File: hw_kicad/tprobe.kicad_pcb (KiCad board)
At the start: 2 copper layers, 15.2 x 44.5 mm, 28 parts, among them IC1 ATTINY85-P, P1 INPUT, P2 PRB_GND, P3 PRB_VCC, P4 AVR_ISP, P5 FTDI_CN, P6 MLIPO, SW1 SW_PUSH_SMALL_H

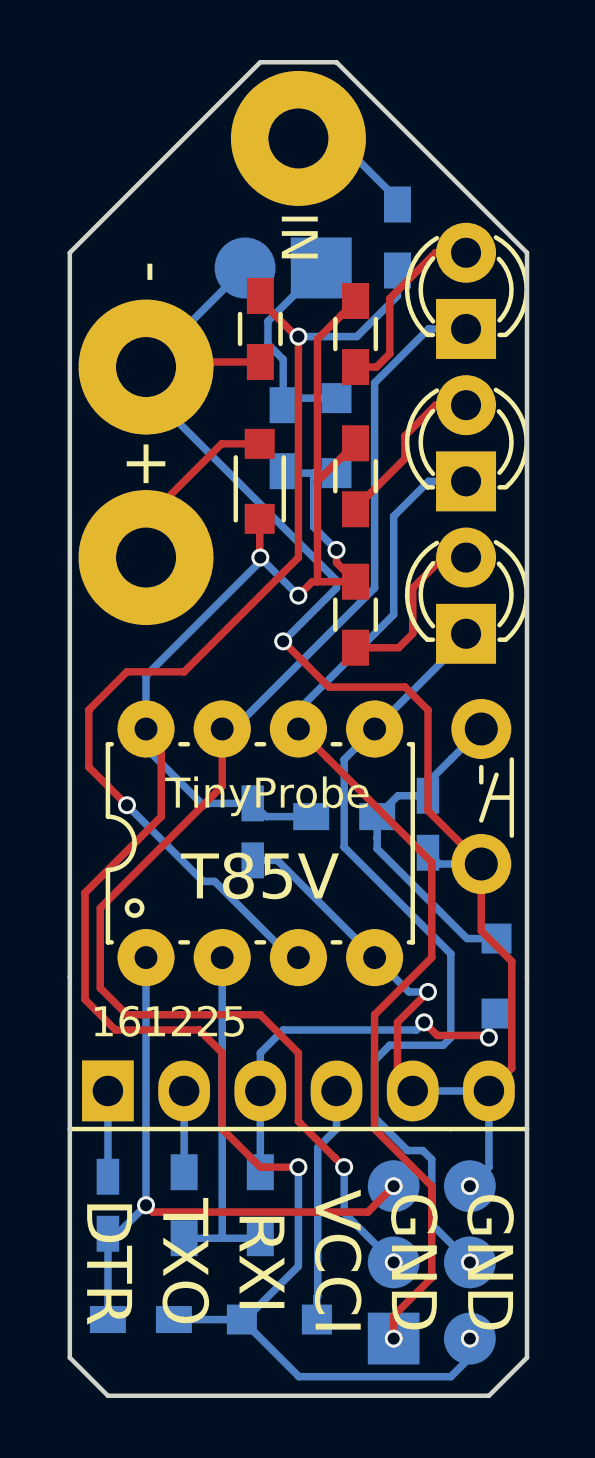
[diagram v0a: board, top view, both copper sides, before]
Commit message: It deserves a real li-ion charger :)
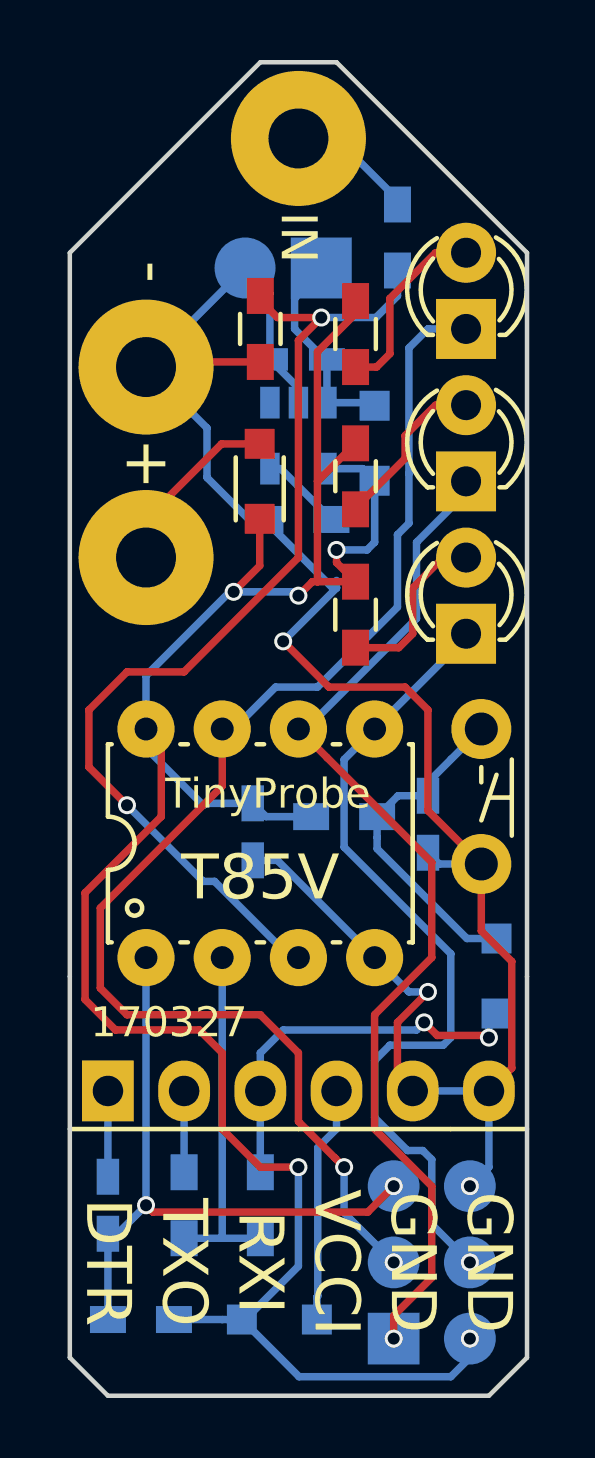
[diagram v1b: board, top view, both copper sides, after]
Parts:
- added C4: 1u, Capacitors_SMD:C_0603_HandSoldering, B.Cu at (148.6, 91.2)
- added U1: TP4055, TO_SOT_Packages_SMD:SOT-23-5, B.Cu at (148.6, 93.7)
- R10: value 100 -> 10k
- moved R10 2.76 mm to (148.6, 96.5), turned to 0 degrees
- moved D7 1.30 mm to (151.1, 94.0)
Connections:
- D7 pad 2: Net-(D7-Pad2) -> Net-(C4-Pad1)
- P6 pad 1: Net-(D7-Pad2) -> Net-(C4-Pad1)
- R10 pad 1: Net-(D7-Pad2) -> GND
- R10 pad 2: VCC -> Net-(R10-Pad2)
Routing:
- net Net-(D7-Pad2): track 7.39 -> 0.00 mm
- net Net-(C4-Pad1): track 0.00 -> 7.35 mm
- net GND: track 60.5 -> 67.1 mm
- net Net-(R10-Pad2): track 0.00 -> 2.75 mm
- net VCC: track 76.0 -> 77.0 mm
- net /SCK_R: track 43.8 -> 44.6 mm
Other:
- board text added: "170327"
- board text removed: "161225"
